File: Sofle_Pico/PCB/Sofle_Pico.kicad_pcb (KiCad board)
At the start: 2 copper layers, 145.4 x 116.3 mm, 123 parts, among them J1 Conn_01x05, J2 4PIN, J3 Conn_01x04, J4 Conn_01x04, J5 Conn_02x05_Odd_Even, J7 Conn_01x04, Q1 Si2301CDS, SW1 SW_PUSH, SW10 SW_PUSH, SW11 SW_PUSH, SW12 SW_PUSH, SW13 SW_PUSH, SW14 SW_PUSH, SW15 SW_PUSH, SW16 SW_PUSH, SW17 SW_PUSH, SW18 SW_PUSH, SW19 SW_PUSH, SW2 SW_PUSH, SW20 SW_PUSH, SW21 SW_PUSH, SW22 SW_PUSH, SW23 SW_PUSH, SW24 SW_PUSH, SW25 Rotary_Encoder_Switch-Device, SW26 SW_PUSH, SW27 SW_PUSH, SW28 SW_PUSH, SW29 SW_PUSH, SW3 SW_PUSH, SW30 SW_PUSH, SW4 SW_PUSH, SW5 SW_PUSH, SW6 SW_PUSH, SW7 SW_PUSH, SW8 SW_PUSH, SW9 SW_PUSH, U2 Pico

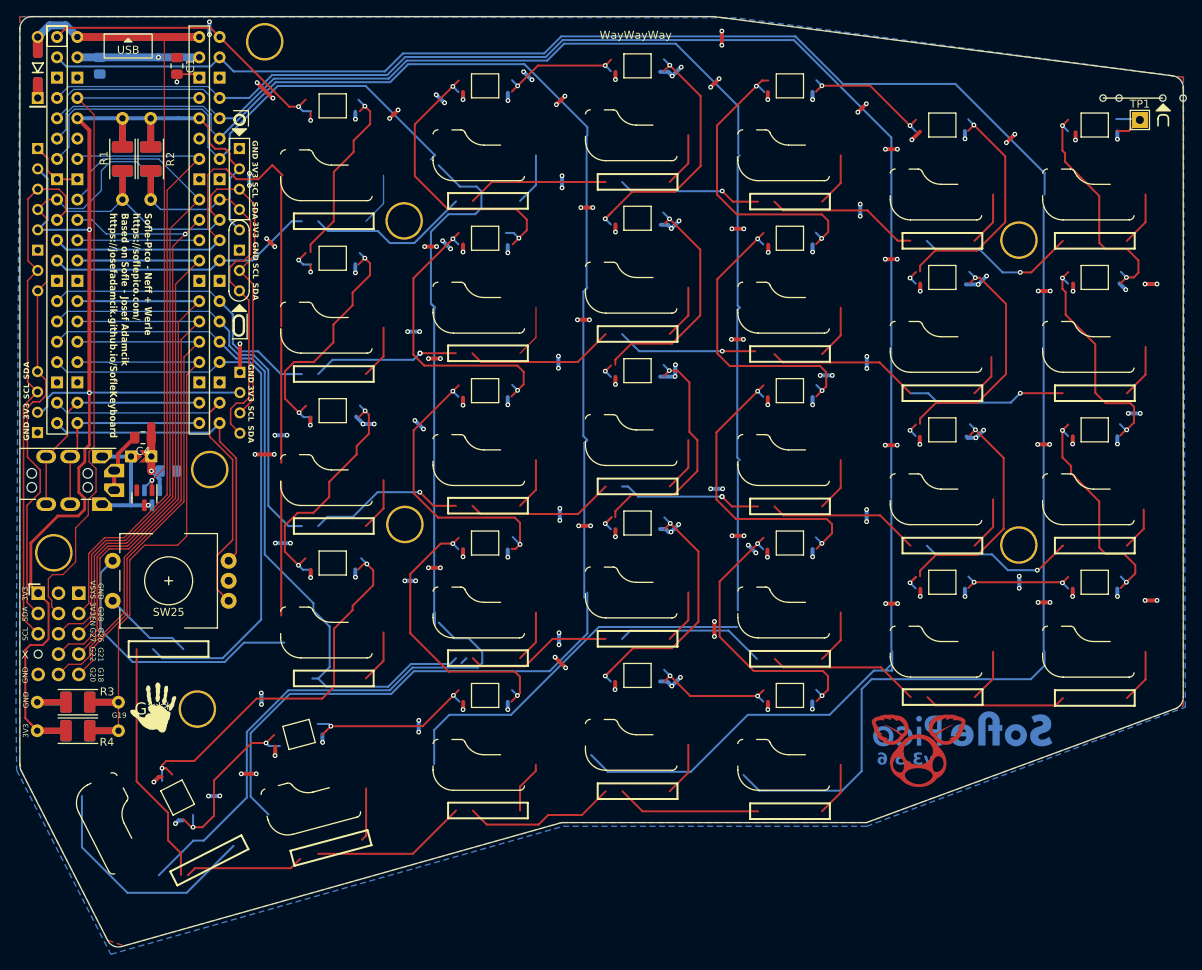
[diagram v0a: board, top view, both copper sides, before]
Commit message: Add a LH version of the component cutout platefoam.
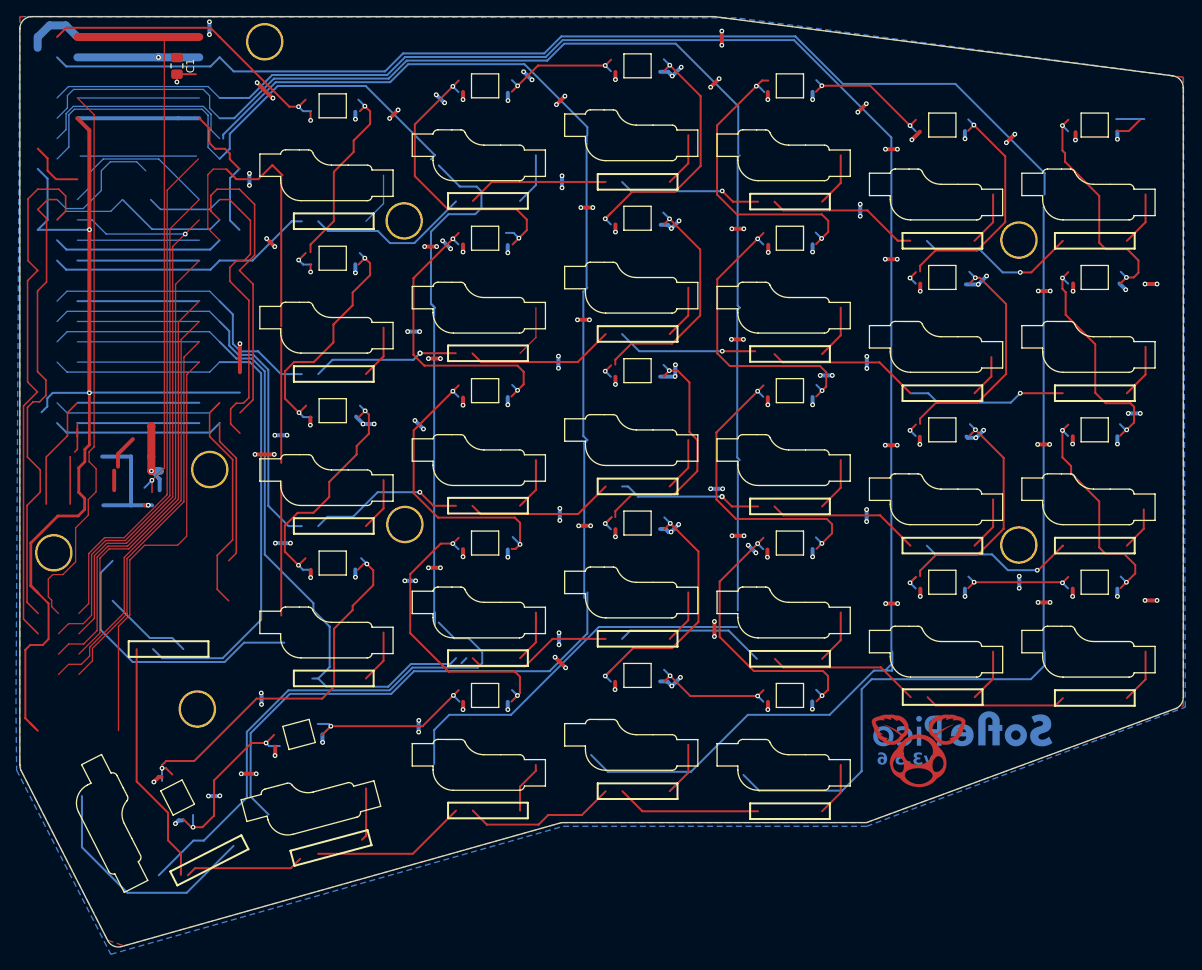
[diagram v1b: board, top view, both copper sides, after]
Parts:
- removed C2, C3, C4: 0.1uF, Capacitor_SMD:C_0805_2012Metric_Pad1.18x1.45mm_HandSolder
- removed D31: MBR120VLSF, Sofle_Pico:D_SOD-123_DO-41_7.62mm_Hybrid_DoubleSided
- removed G***: LOGO, Sofle_Pico:RH_Print_Logo
- removed G***: LOGO, Sofle_Pico:LH_Print
- removed J1: Conn_01x05, Sofle_Pico:Pimaroni_PinHeader_1x05_P2.54mm_Vertical Sofle v3b
- removed J2: 4PIN, Sofle_Pico:MJ-4PP-9
- removed J3: Conn_01x04, Sofle_Pico:OLED SSD1306 128x64
- removed J4, J7: Conn_01x04, Sofle_Pico:Cirque tie in
- removed J5: Conn_02x05_Odd_Even, Connector_PinHeader_2.54mm:PinHeader_2x05_P2.54mm_Vertical
- removed JP2: SolderJumper_2_Open, Sofle_Pico:Level Shifter Bypass Jumper
- removed Q1: Si2301CDS, Sofle_Pico:SOT-23_DS
- removed R1, R2, R3, R4: 2.2k, Sofle_Pico:Res_1206_SMD_6.3mm_TH_Hybrid
- removed the REF** at (226.8, 44.2)
- removed the REF** at (96.2, 68.5)
- removed SW25: Rotary_Encoder_Switch-Device, Sofle_Pico:RotaryEncoder_Alps_EC11E-Switch_Vertical_H20mm-keebio_modified
- removed TP1: TestPoint, TestPoint:TestPoint_THTPad_2.0x2.0mm_Drill1.0mm
- removed U2: Pico, Sofle_Pico:RPi_Pico_SMD_TH_DS
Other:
- board text removed: "${REFERENCE}"
- board text removed: "3V3"
- board text removed: "3V3EN"
- board text removed: "G18"
- board text removed: "G19"
- board text removed: "G20"
- board text removed: "G21"
- board text removed: "G22"
- board text removed: "G26"
- board text removed: "G27"
- board text removed: "G28"
- board text removed: "GND"
- board text removed: "LH"
- board text removed: "RH"
- board text removed: "SCL"
- board text removed: "SDA"
- board text removed: "Sofle-Pico - Neff + Werle https://soflepico.com/ Based on Sofle - Josef Adamcik https://josefadamcik.github.io/SofleKeyboard"
- board text removed: "USB"
- board text removed: "VSYS"
- board text removed: "WayWayWay"
- board text removed: "X"
